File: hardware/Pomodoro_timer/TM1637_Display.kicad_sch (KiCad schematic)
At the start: 3 parts, among them U4 CC56-12EWA, U5 TM1637

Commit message: PCB Ver.A : The Schematic completed the next part for PCB can be started.
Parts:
- added R6, R7: 1K, symbol Device:R_Small
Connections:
- net PWR: now also R6.1, R7.1
- net DIO: now reaches U5.17 (DIO)
- net DIO: now also R7.2
- net CLK: now reaches U5.18 (CLK)
- net CLK: now also R6.2

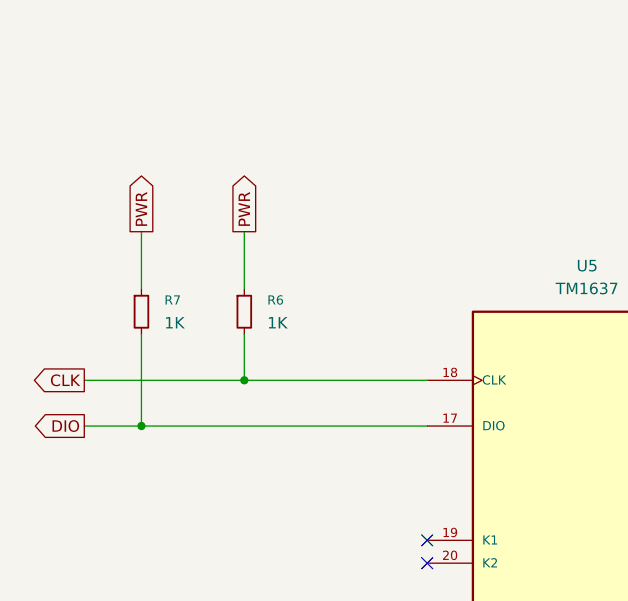
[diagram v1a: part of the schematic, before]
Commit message: PCB Ver.A The required changes were not in line So made few alterations Need to start again
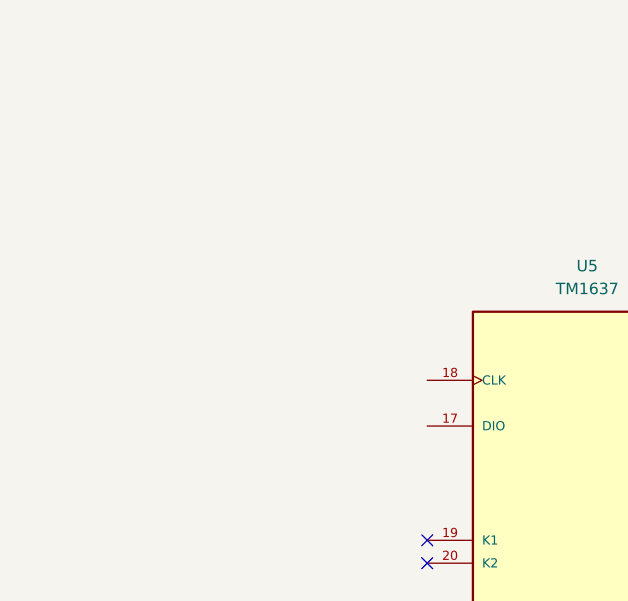
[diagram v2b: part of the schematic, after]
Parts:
- removed R6, R7: 1K, symbol Device:R_Small
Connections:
- net CLK: no longer names the net of U5.18 (CLK)
- net DIO: no longer names the net of U5.17 (DIO)
